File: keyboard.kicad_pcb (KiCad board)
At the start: 2 copper layers, 192 parts, among them SW1 SW_Push, U1 ATmega32U4-AU, Y1 16MHz

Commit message: Imported autocad layout and aligned upper left key to grid origin
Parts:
- moved C1 210.5 mm to (92.1, 288.1)
- moved D10 210.5 mm to (215.1, 360.1)
- moved D11 210.5 mm to (246.8, 329.9)
- moved D15 210.5 mm to (261.3, 316.4)
- moved D26 210.5 mm to (255.5, 316.4)
- moved D29 210.5 mm to (241.1, 329.9)
- moved D31 210.5 mm to (314.9, 259.1)
- moved D4 210.5 mm to (33.3, 372.2)
- moved D48 210.5 mm to (235.3, 329.9)
- moved D71 210.5 mm to (108.1, 372.2)
- moved D72 210.5 mm to (102.3, 372.2)
- moved D73 210.5 mm to (96.6, 372.2)
- moved D74 210.5 mm to (90.8, 372.2)
- moved D75 210.5 mm to (85.1, 372.2)
- moved D76 210.5 mm to (79.3, 372.2)
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
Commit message: Aligned keys in pcb
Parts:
- moved MX_XR2 406.9 mm to (314.3, 19.1)
- moved MX_XR1 386.6 mm to (314.3, 0.00)
- moved MX_ESC1 377.3 mm to (23.8, 0.00)
- moved MX_FN5 359.2 mm to (142.9, 0.00)
- moved MX_BSLASH1 356.3 mm to (23.8, 19.1)
- moved MX_0 356.0 mm to (214.3, 19.1)
- moved MX_5 349.5 mm to (119.1, 19.1)
- moved MX_XL1 342.6 mm to (0.00, 0.00)
- moved MX_4 341.9 mm to (100.0, 19.1)
- moved MX_FN7 340.6 mm to (181.0, 0.00)
- moved MX_3 339.9 mm to (81.0, 19.1)
- moved MX_BSPACE1 332.9 mm to (281.0, 19.1)
- moved MX_Y1 329.2 mm to (147.6, 38.1)
- moved MX_R1 326.0 mm to (109.5, 38.1)
- moved MX_FN1 325.0 mm to (52.4, 0.00)
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
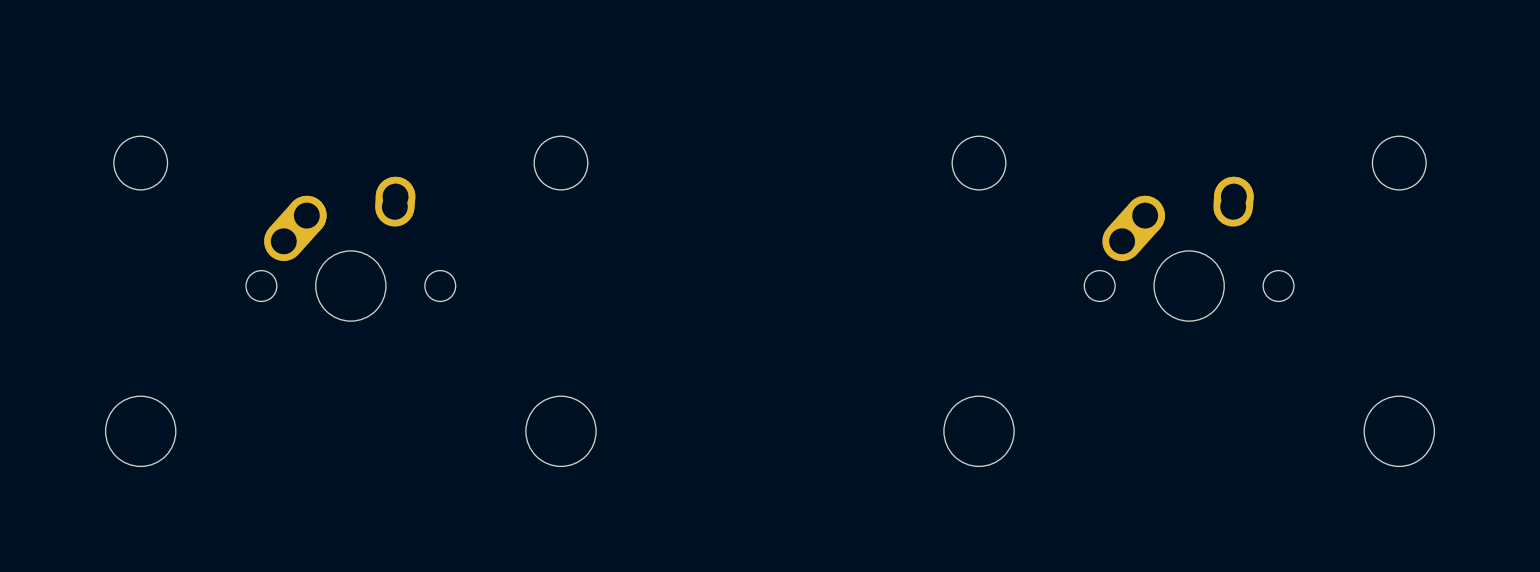
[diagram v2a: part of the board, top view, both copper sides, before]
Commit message: Reversed stabilizers for spacebars
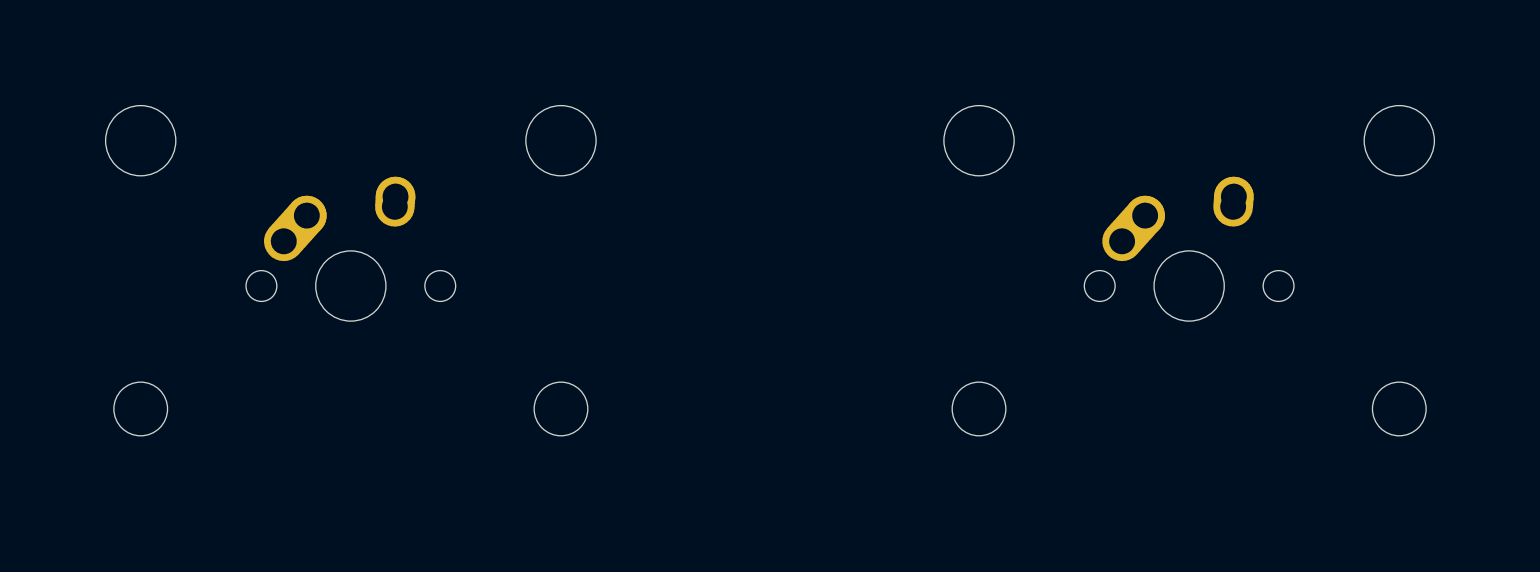
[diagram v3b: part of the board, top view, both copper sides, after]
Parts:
- MX_LSPACE1: footprint MX_Alps_Hybrid:MX-2.75U-NoLED -> MX_Alps_Hybrid:MX-2.75U-ReversedStabilizers-NoLED
- MX_RSPACE1: footprint MX_Alps_Hybrid:MX-2.25U-NoLED -> MX_Alps_Hybrid:MX-2.25U-ReversedStabilizers-NoLED

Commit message: Positioning components on pcb
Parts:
- C1, C2, C3, C4, C5, C6, C7, D1, D10, D11, D12, D13, D14, D15, D16, D17, D18, D19, D2, D20, D21, D22, D23, D24, D25, D26, D27, D28, D29, D3, D30, D31, D32, D33, D34, D35, D36, D37, D38, D39, D4, D40, D41, D42, D43, D44, D45, D46, D47, D48, D49, D5, D50, D51, D52, D53, D54, D55, D56, D57, D58, D59, D6, D60, D61, D62, D63, D64, D65, D66, D67, D68, D69, D7, D70, D71, D72, D73, D74, D75, D76, D77, D78, D79, D8, D80, D81, D82, D83, D84, D85, D86, D87, D88, D9, F1, R1, R2, R3, R4, SW1, U1, USB1, Y1: moved to B.Cu
- moved D79 391.9 mm to (298.4, 0.00), turned to 90 degrees
- moved D80 375.5 mm to (288.9, 19.1), turned to 90 degrees
- moved D75 364.7 mm to (279.4, 0.06), turned to 90 degrees
- moved D81 364.6 mm to (296.1, 48.5), turned to 90 degrees
- moved D82 353.5 mm to (298.4, 76.3), turned to 90 degrees
- moved D83 347.2 mm to (298.4, 95.2), turned to 90 degrees
- moved D71 340.6 mm to (260.4, 0.00), turned to 90 degrees
- moved D72 327.9 mm to (260.4, 19.1), turned to 90 degrees
- moved D77 326.2 mm to (274.6, 57.1), turned to 90 degrees
- moved D74 325.5 mm to (269.9, 38.1), turned to 90 degrees
- moved D1 317.7 mm to (7.94, 0.00), turned to 90 degrees
- moved D7 311.1 mm to (31.8, 0.00), turned to 90 degrees
- moved D85 310.5 mm to (322.3, 0.00), turned to 90 degrees
- moved D65 309.6 mm to (241.3, 0.06), turned to 90 degrees
- moved D78 308.6 mm to (279.4, 95.2), turned to 90 degrees
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
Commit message: Place components on pcb
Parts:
- moved SW1 350.4 mm to (316.0, 73.8), turned to 0 degrees
- moved R3 296.7 mm to (315.8, 81.5)
- moved F1 292.7 mm to (213.7, 3.94)
- moved R2 266.5 mm to (222.6, 3.30), turned to 90 degrees
- moved R1 265.8 mm to (218.2, 3.30), turned to 90 degrees
- moved USB1 259.7 mm to (216.8, -7.87), turned to 270 degrees
- moved R4 238.7 mm to (261.6, 99.2), turned to 90 degrees
- moved C4 235.4 mm to (256.4, 83.6), turned to 90 degrees
- moved C5 229.8 mm to (248.3, 103.4), turned to 180 degrees
- moved C6 229.0 mm to (254.1, 103.4), turned to 180 degrees
- moved C7 227.4 mm to (239.6, 95.2), turned to 180 degrees
- moved C3 221.7 mm to (245.4, 83.6), turned to 90 degrees
- moved C2 209.9 mm to (239.8, 89.9), turned to 90 degrees
- moved C1 207.2 mm to (235.7, 89.9)
- moved U1 9.41 mm to (251.3, 94.2)
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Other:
- board outline added: 333.4 x 114.3 mm

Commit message: Placement and prepare for routing
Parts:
- moved R3 79.5 mm to (236.6, 88.3), turned to 270 degrees
- moved C1 25.7 mm to (261.4, 90.3)
- moved C5 6.10 mm to (254.4, 103.3)
- moved C6 5.84 mm to (248.3, 103.3), turned to 0 degrees
- moved C2 1.78 mm to (241.6, 90.0)
- moved C7 0.51 mm to (240.2, 95.2)
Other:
- net class Default: trace_width 0.25 -> 0.254
- net class Power added: clearance 0.2, trace_width 0.381, via_dia 0.8, via_drill 0.4
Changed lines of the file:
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@@
   )
   (setup
-    (last_trace_width 0.25)
+    (last_trace_width 0.254)
     (trace_clearance 0.2)
     (zone_clearance 0.508)
@@
   (net_class Default "This is the default net class."
     (clearance 0.2)
-    (trace_width 0.25)
+    (trace_width 0.254)
     (via_dia 0.8)
     (via_drill 0.4)
     (uvia_dia 0.3)
     (uvia_drill 0.1)
-    (add_net +5V)
     (add_net COL0)
     (add_net COL1)
@@
     (add_net D+)
     (add_net D-)
-    (add_net GND)
     (add_net "Net-(C3-Pad1)")
     (add_net "Net-(C4-Pad1)")
@@
     (add_net ROW4)
     (add_net ROW5)
+  )
+  (net_class Power ""
+    (clearance 0.2)
+    (trace_width 0.381)
+    (via_dia 0.8)
+    (via_drill 0.4)
+    (uvia_dia 0.3)
+    (uvia_drill 0.1)
+    (add_net +5V)
+    (add_net GND)
     (add_net VCC)
   )
@@
   )
   (module Resistor_SMD:R_0805_2012Metric (layer B.Cu)
-    (at 315.849 81.534)
+    (at 236.601 88.265 270)
     (descr "Resistor SMD 0805 (2012 Metric), square (rectangular) end terminal, IPC_7351 nominal, (Body size source: https://docs.google.com/spreadsheets/d/1BsfQQcO9C6DZCsRaXUlFlo91Tg2WpOkGARC1WS5S8t0/edit?usp=sharing), generated with kicad-footprint-generator")
     (tags resistor)
     (attr smd)
-    (fp_text reference R3 (at 0 1.65) (layer B.SilkS)
+    (fp_text reference R3 (at 0 1.65 90) (layer B.SilkS)
       (effects (font (size 1 1) (thickness 0.15)) (justify mirror))
     )
-    (fp_text value 10k (at 0 -1.65) (layer B.Fab)
+    (fp_text value 10k (at 0 -1.65 90) (layer B.Fab)
       (effects (font (size 1 1) (thickness 0.15)) (justify mirror))
     )
-    (fp_text user %R (at 0 0) (layer B.Fab)
+    (fp_text user %R (at 0 0 90) (layer B.Fab)
       (effects (font (size 0.5 0.5) (thickness 0.08)) (justify mirror))
     )
@@
     (fp_line (start -1 0.6) (end 1 0.6) (layer B.Fab) (width 0.1))
     (fp_line (start -1 -0.6) (end -1 0.6) (layer B.Fab) (width 0.1))
-    (pad 2 smd roundrect (at 0.9375 0) (size 0.975 1.4) (layers B.Cu B.Paste B.Mask) (roundrect_rratio 0.25)
+    (pad 2 smd roundrect (at 0.9375 0 270) (size 0.975 1.4) (layers B.Cu B.Paste B.Mask) (roundrect_rratio 0.25)
       (net 2 +5V))
-    (pad 1 smd roundrect (at -0.9375 0) (size 0.975 1.4) (layers B.Cu B.Paste B.Mask) (roundrect_rratio 0.25)
+    (pad 1 smd roundrect (at -0.9375 0 270) (size 0.975 1.4) (layers B.Cu B.Paste B.Mask) (roundrect_rratio 0.25)
       (net 122 "Net-(R3-Pad1)"))
     (model ${KISYS3DMOD}/Resistor_SMD.3dshapes/R_0805_2012Metric.wrl
@@
   )
   (module Capacitor_SMD:C_0805_2012Metric (layer B.Cu)
-    (at 239.649 95.25 180)
+    (at 240.157 95.25 180)
     (descr "Capacitor SMD 0805 (2012 Metric), square (rectangular) end terminal, IPC_7351 nominal, (Body size source: https://docs.google.com/spreadsheets/d/1BsfQQcO9C6DZCsRaXUlFlo91Tg2WpOkGARC1WS5S8t0/edit?usp=sharing), generated with kicad-footprint-generator")
     (tags capacitor)
@@
   )
   (module Capacitor_SMD:C_0805_2012Metric (layer B.Cu)
-    (at 254.127 103.378 180)
+    (at 248.285 103.251)
     (descr "Capacitor SMD 0805 (2012 Metric), square (rectangular) end terminal, IPC_7351 nominal, (Body size source: https://docs.google.com/spreadsheets/d/1BsfQQcO9C6DZCsRaXUlFlo91Tg2WpOkGARC1WS5S8t0/edit?usp=sharing), generated with kicad-footprint-generator")
     (tags capacitor)
@@
     (fp_line (start -1 0.6) (end 1 0.6) (layer B.Fab) (width 0.1))
     (fp_line (start -1 -0.6) (end -1 0.6) (layer B.Fab) (width 0.1))
-    (pad 2 smd roundrect (at 0.9375 0 180) (size 0.975 1.4) (layers B.Cu B.Paste B.Mask) (roundrect_rratio 0.25)
+    (pad 2 smd roundrect (at 0.9375 0) (size 0.975 1.4) (layers B.Cu B.Paste B.Mask) (roundrect_rratio 0.25)
       (net 1 GND))
-    (pad 1 smd roundrect (at -0.9375 0 180) (size 0.975 1.4) (layers B.Cu B.Paste B.Mask) (roundrect_rratio 0.25)
+    (pad 1 smd roundrect (at -0.9375 0) (size 0.975 1.4) (layers B.Cu B.Paste B.Mask) (roundrect_rratio 0.25)
       (net 2 +5V))
     (model ${KISYS3DMOD}/Capacitor_SMD.3dshapes/C_0805_2012Metric.wrl
@@
   )
   (module Capacitor_SMD:C_0805_2012Metric (layer B.Cu)
-    (at 248.285 103.378 180)
+    (at 254.381 103.251 180)
     (descr "Capacitor SMD 0805 (2012 Metric), square (rectangular) end terminal, IPC_7351 nominal, (Body size source: https://docs.google.com/spreadsheets/d/1BsfQQcO9C6DZCsRaXUlFlo91Tg2WpOkGARC1WS5S8t0/edit?usp=sharing), generated with kicad-footprint-generator")
     (tags capacitor)
@@
   )
   (module Capacitor_SMD:C_0805_2012Metric (layer B.Cu)
-    (at 239.776 89.916 90)
+    (at 241.554 90.043 90)
     (descr "Capacitor SMD 0805 (2012 Metric), square (rectangular) end terminal, IPC_7351 nominal, (Body size source: https://docs.google.com/spreadsheets/d/1BsfQQcO9C6DZCsRaXUlFlo91Tg2WpOkGARC1WS5S8t0/edit?usp=sharing), generated with kicad-footprint-generator")
     (tags capacitor)
@@
   )
   (module Capacitor_SMD:C_0805_2012Metric (layer B.Cu)
-    (at 235.712 89.916 90)
+    (at 261.366 90.297 90)
     (descr "Capacitor SMD 0805 (2012 Metric), square (rectangular) end terminal, IPC_7351 nominal, (Body size source: https://docs.google.com/spreadsheets/d/1BsfQQcO9C6DZCsRaXUlFlo91Tg2WpOkGARC1WS5S8t0/edit?usp=sharing), generated with kicad-footprint-generator")
     (tags capacitor)

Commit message: Unknown changes
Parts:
- moved C6 8.64 mm to (240.4, 99.7), turned to 270 degrees
- moved R2 5.21 mm to (217.4, 3.56)
- moved F1 3.53 mm to (210.7, 5.71)
- moved R1 2.93 mm to (215.3, 3.56)
- moved C7 1.35 mm to (241.0, 94.2)
- moved Y1 0.33 mm to (251.3, 83.6), turned to 0 degrees
- turned C3 to 270 degrees
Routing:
- net +5V: track 0.00 -> 117.2 mm, vias 0 -> 1
- net Net-(R1-Pad1): track 0.00 -> 116.0 mm
- net Net-(R2-Pad1): track 0.00 -> 114.5 mm
- net GND: track 0.00 -> 44.4 mm
- net Net-(C3-Pad1): track 0.00 -> 26.0 mm
- net Net-(C4-Pad1): track 0.00 -> 8.92 mm
- net D-: track 0.00 -> 6.29 mm
- net D+: track 0.00 -> 6.26 mm
- net Net-(R4-Pad2): track 0.00 -> 4.59 mm
- net VCC: track 0.00 -> 3.55 mm
